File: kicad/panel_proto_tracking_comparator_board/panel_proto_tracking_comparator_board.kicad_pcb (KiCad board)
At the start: 2 copper layers, 102 x 67.5 mm, 570 parts, among them U1 TLV3542, U2 MCP6566

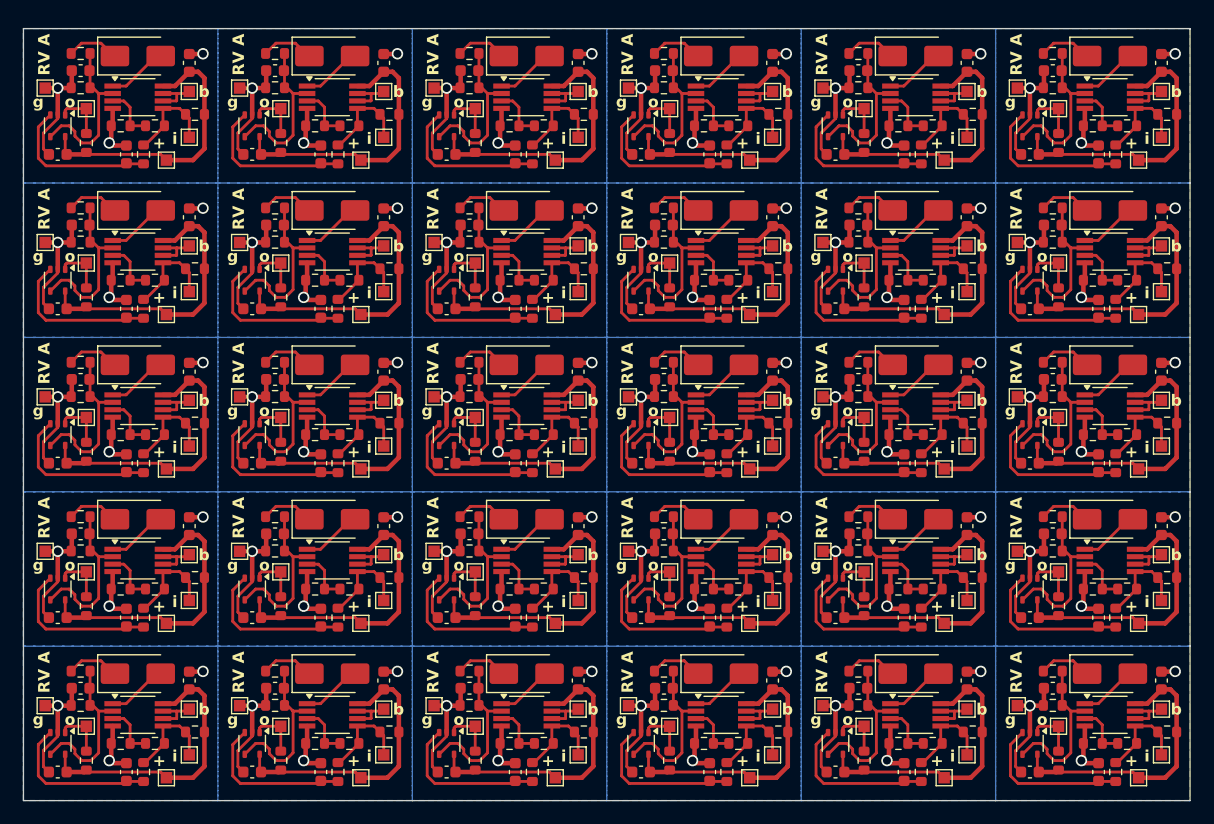
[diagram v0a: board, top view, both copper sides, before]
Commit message: Save bodge board rev B and additional sims
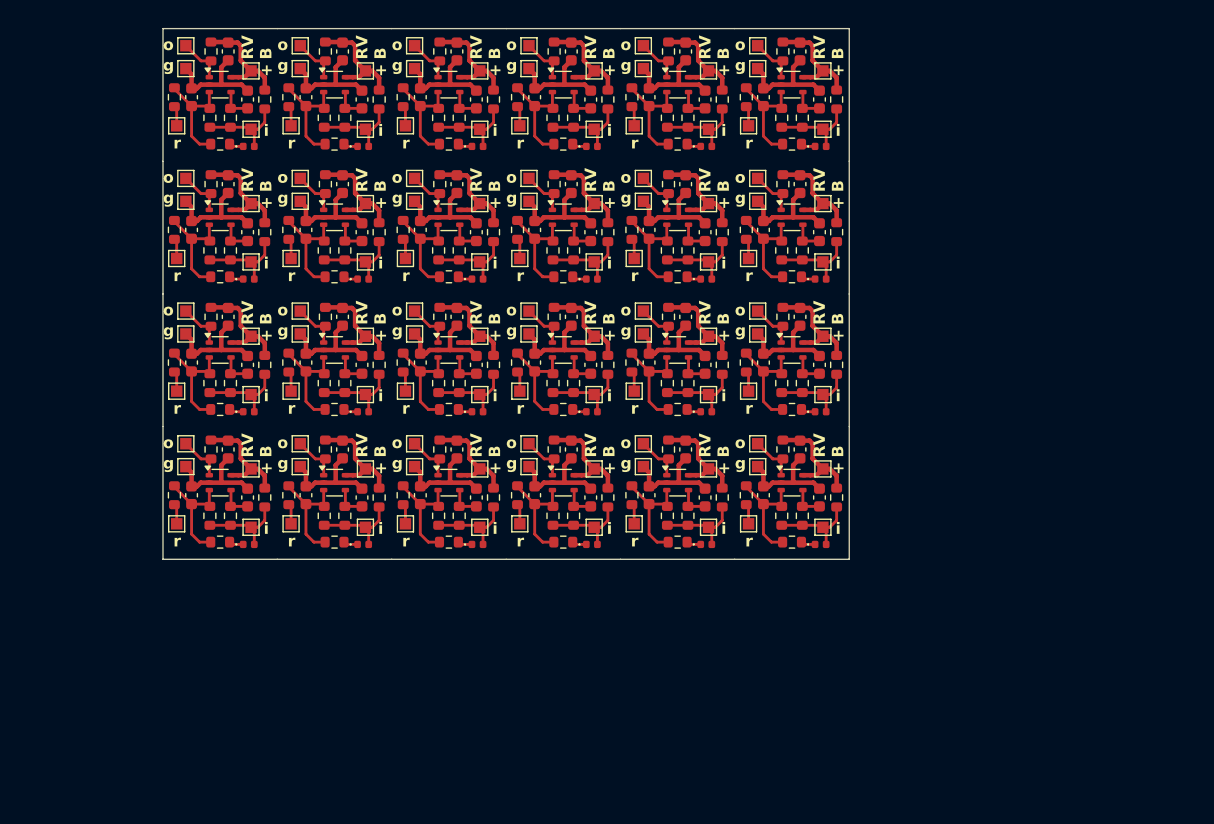
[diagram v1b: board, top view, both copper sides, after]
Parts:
- removed the C1 at (146.0, 23.0)
- removed the C1 at (197.0, 50.0)
- removed the C1 at (163.0, 36.5)
- removed the C1 at (112.0, 77.0)
- removed the C1 at (163.0, 50.0)
- removed the C1 at (163.0, 63.5)
- removed the C1 at (146.0, 63.5)
- removed the C1 at (180.0, 77.0)
- removed the C1 at (146.0, 77.0)
- removed the C1 at (163.0, 77.0)
- removed the C1 at (146.0, 36.5)
- removed the C1 at (197.0, 36.5)
- removed the C1 at (146.0, 50.0)
- removed the C1 at (129.0, 77.0)
- removed the C1 at (129.0, 36.5)
- removed the C1 at (197.0, 63.5)
- removed the C1 at (163.0, 23.0)
- removed the C1 at (112.0, 63.5)
- removed the C1 at (112.0, 23.0)
- removed the C1 at (180.0, 23.0)
- removed the C1 at (197.0, 23.0)
- removed the C1 at (129.0, 50.0)
- removed the C1 at (112.0, 50.0)
- removed the C1 at (180.0, 63.5)
- removed the C1 at (180.0, 50.0)
- removed the C1 at (129.0, 23.0)
- removed the C1 at (129.0, 63.5)
- removed the C1 at (197.0, 77.0)
- removed the C1 at (112.0, 36.5)
- removed the C1 at (180.0, 36.5)
- removed the C2 at (153.5, 77.7)
- removed the C2 at (136.5, 23.7)
- removed the C2 at (170.5, 50.7)
- removed the C2 at (102.5, 64.2)
- removed the C2 at (119.5, 50.7)
- removed the C2 at (102.5, 50.7)
- removed the C2 at (170.5, 77.7)
- removed the C2 at (102.5, 37.2)
- removed the C2 at (187.5, 77.7)
- removed the C2 at (153.5, 23.7)
- removed the C2 at (170.5, 23.7)
- removed the C2 at (187.5, 50.7)
- removed the C2 at (119.5, 64.2)
- removed the C2 at (170.5, 64.2)
- removed the C2 at (153.5, 37.2)
- removed the C2 at (119.5, 23.7)
- removed the C2 at (187.5, 23.7)
- removed the C2 at (136.5, 64.2)
- removed the C2 at (187.5, 37.2)
- removed the C2 at (102.5, 23.7)
- removed the C2 at (136.5, 50.7)
- removed the C2 at (153.5, 64.2)
- removed the C2 at (136.5, 37.2)
- removed the C2 at (102.5, 77.7)
- removed the C2 at (153.5, 50.7)
- removed the C2 at (119.5, 77.7)
- removed the C2 at (187.5, 64.2)
- removed the C2 at (170.5, 37.2)
- removed the C2 at (119.5, 37.2)
- removed the C2 at (136.5, 77.7)
- removed the C3 at (191.5, 71.5)
- removed the C3 at (157.5, 71.5)
- removed the C3 at (174.5, 44.5)
- removed the C3 at (174.5, 85.0)
- removed the C3 at (123.5, 31.0)
- removed the C3 at (106.5, 31.0)
- removed the C3 at (157.5, 44.5)
- removed the C3 at (191.5, 31.0)
- removed the C3 at (123.5, 71.5)
- removed the C3 at (140.5, 85.0)
- removed the C3 at (174.5, 31.0)
- removed the C3 at (174.5, 58.0)
- removed the C3 at (174.5, 71.5)
- removed the C3 at (140.5, 31.0)
- removed the C3 at (191.5, 85.0)
- removed the C3 at (106.5, 71.5)
- removed the C3 at (191.5, 44.5)
- removed the C3 at (123.5, 58.0)
- removed the C3 at (157.5, 31.0)
- removed the C3 at (123.5, 85.0)
- removed the C3 at (106.5, 58.0)
- removed the C3 at (106.5, 85.0)
- removed the C3 at (140.5, 44.5)
- removed the C3 at (157.5, 58.0)
- removed the C3 at (157.5, 85.0)
- removed the C3 at (140.5, 58.0)
- removed the C3 at (123.5, 44.5)
- removed the C3 at (191.5, 58.0)
- removed the C3 at (106.5, 44.5)
- removed the C3 at (140.5, 71.5)
- removed C4 (x30): 0.1uF, Capacitor_SMD:C_0603_1608Metric
- removed the D1 at (158.5, 62.9)
- removed the D1 at (175.5, 76.4)
- removed the D1 at (175.5, 49.4)
- removed the D1 at (192.5, 22.4)
- removed the D1 at (141.5, 62.9)
- removed the D1 at (158.5, 35.9)
- removed the D1 at (124.5, 76.4)
- removed the D1 at (124.5, 22.4)
- removed the D1 at (107.5, 49.4)
- removed the D1 at (192.5, 76.4)
- removed the D1 at (158.5, 22.4)
- removed the D1 at (192.5, 62.9)
- removed the D1 at (124.5, 49.4)
- removed the D1 at (192.5, 35.9)
- removed the D1 at (141.5, 22.4)
- removed the D1 at (124.5, 35.9)
- removed the D1 at (175.5, 22.4)
- removed the D1 at (175.5, 62.9)
- removed the D1 at (192.5, 49.4)
- removed the D1 at (141.5, 76.4)
- removed the D1 at (141.5, 35.9)
- removed the D1 at (141.5, 49.4)
- removed the D1 at (107.5, 62.9)
- removed the D1 at (107.5, 35.9)
- removed the D1 at (107.5, 22.4)
- removed the D1 at (158.5, 49.4)
- removed the D1 at (175.5, 35.9)
- removed the D1 at (158.5, 76.4)
- removed the D1 at (124.5, 62.9)
- removed the D1 at (107.5, 76.4)
- removed the R1 at (129.5, 27.5)
- removed the R1 at (180.5, 41.0)
- removed the R1 at (163.5, 27.5)
- removed the R1 at (197.5, 41.0)
- removed the R1 at (112.5, 41.0)
- removed the R1 at (163.5, 68.0)
- removed the R1 at (197.5, 68.0)
- removed the R1 at (129.5, 41.0)
- removed the R1 at (112.5, 68.0)
- removed the R1 at (146.5, 81.5)
- removed the R1 at (197.5, 54.5)
- removed the R1 at (197.5, 81.5)
- removed the R1 at (129.5, 81.5)
- removed the R1 at (146.5, 41.0)
- removed the R1 at (180.5, 68.0)
- removed the R1 at (146.5, 27.5)
- removed the R1 at (112.5, 27.5)
- removed the R1 at (180.5, 81.5)
- removed the R1 at (163.5, 54.5)
- removed the R1 at (163.5, 81.5)
- removed the R1 at (112.5, 81.5)
- removed the R1 at (163.5, 41.0)
- removed the R1 at (146.5, 54.5)
- removed the R1 at (180.5, 54.5)
- removed the R1 at (129.5, 54.5)
- removed the R1 at (197.5, 27.5)
- removed the R1 at (180.5, 27.5)
- removed the R1 at (129.5, 68.0)
- removed the R1 at (146.5, 68.0)
- removed the R1 at (112.5, 54.5)
- removed the R2 at (126.0, 82.5)
- removed the R2 at (126.0, 42.0)
- removed the R2 at (194.0, 42.0)
- removed the R2 at (109.0, 28.5)
- removed the R2 at (177.0, 42.0)
- removed the R2 at (126.0, 69.0)
- removed the R2 at (160.0, 28.5)
- removed the R2 at (143.0, 55.5)
- removed the R2 at (109.0, 69.0)
- removed the R2 at (143.0, 69.0)
- removed the R2 at (126.0, 55.5)
- removed the R2 at (160.0, 42.0)
- removed the R2 at (126.0, 28.5)
- removed the R2 at (143.0, 42.0)
- removed the R2 at (109.0, 42.0)
- removed the R2 at (177.0, 82.5)
- removed the R2 at (109.0, 55.5)
- removed the R2 at (160.0, 82.5)
- removed the R2 at (194.0, 28.5)
- removed the R2 at (143.0, 28.5)
- removed the R2 at (194.0, 69.0)
- removed the R2 at (177.0, 69.0)
- removed the R2 at (177.0, 28.5)
- removed the R2 at (109.0, 82.5)
- removed the R2 at (160.0, 69.0)
- removed the R2 at (160.0, 55.5)
- removed the R2 at (194.0, 82.5)
- removed the R2 at (143.0, 82.5)
- removed the R2 at (177.0, 55.5)
- removed the R2 at (194.0, 55.5)
- removed the R3 at (157.0, 28.5)
- removed the R3 at (106.0, 42.0)
- removed the R3 at (123.0, 28.5)
- removed the R3 at (191.0, 28.5)
- removed the R3 at (140.0, 42.0)
- removed the R3 at (157.0, 42.0)
- removed the R3 at (157.0, 69.0)
- removed the R3 at (174.0, 69.0)
- removed the R3 at (140.0, 55.5)
- removed the R3 at (191.0, 55.5)
- removed the R3 at (157.0, 82.5)
- removed the R3 at (106.0, 69.0)
- removed the R3 at (157.0, 55.5)
- removed the R3 at (106.0, 55.5)
- removed the R3 at (191.0, 42.0)
- removed the R3 at (140.0, 28.5)
- removed the R3 at (123.0, 69.0)
- removed the R3 at (191.0, 69.0)
- removed the R3 at (123.0, 42.0)
- removed the R3 at (140.0, 82.5)
- removed the R3 at (191.0, 82.5)
- removed the R3 at (174.0, 55.5)
- removed the R3 at (106.0, 82.5)
- removed the R3 at (123.0, 55.5)
- removed the R3 at (174.0, 82.5)
- removed the R3 at (106.0, 28.5)
- removed the R3 at (123.0, 82.5)
- removed the R3 at (174.0, 28.5)
- removed the R3 at (140.0, 69.0)
- removed the R3 at (174.0, 42.0)
- removed the R4 at (119.5, 35.7)
- removed the R4 at (102.5, 49.2)
- removed the R4 at (170.5, 35.7)
- removed the R4 at (136.5, 35.7)
- removed the R4 at (170.5, 62.7)
- removed the R4 at (136.5, 62.7)
- removed the R4 at (136.5, 49.2)
- removed the R4 at (119.5, 62.7)
- removed the R4 at (187.5, 62.7)
- removed the R4 at (119.5, 22.2)
- removed the R4 at (153.5, 62.7)
- removed the R4 at (102.5, 76.2)
- removed the R4 at (170.5, 22.2)
- removed the R4 at (119.5, 49.2)
- removed the R4 at (136.5, 22.2)
- removed the R4 at (153.5, 49.2)
- removed the R4 at (153.5, 35.7)
- removed the R4 at (187.5, 22.2)
- removed the R4 at (136.5, 76.2)
- removed the R4 at (170.5, 76.2)
- removed the R4 at (153.5, 22.2)
- removed the R4 at (102.5, 62.7)
- removed the R4 at (187.5, 35.7)
- removed the R4 at (187.5, 49.2)
- removed the R4 at (102.5, 35.7)
- removed the R4 at (187.5, 76.2)
- removed the R4 at (102.5, 22.2)
- removed the R4 at (153.5, 76.2)
- removed the R4 at (170.5, 49.2)
- removed the R4 at (119.5, 76.2)
- removed the R5 at (170.5, 25.2)
- removed the R5 at (187.5, 25.2)
- removed the R5 at (102.5, 25.2)
- removed the R5 at (153.5, 38.7)
- removed the R5 at (170.5, 52.2)
- removed the R5 at (102.5, 52.2)
- removed the R5 at (153.5, 52.2)
- removed the R5 at (153.5, 65.7)
- removed the R5 at (187.5, 65.7)
- removed the R5 at (119.5, 38.7)
- removed the R5 at (102.5, 79.2)
- removed the R5 at (187.5, 38.7)
- removed the R5 at (119.5, 25.2)
- removed the R5 at (170.5, 65.7)
- removed the R5 at (102.5, 38.7)
- removed the R5 at (187.5, 52.2)
- removed the R5 at (119.5, 79.2)
- removed the R5 at (187.5, 79.2)
- removed the R5 at (136.5, 65.7)
- removed the R5 at (119.5, 52.2)
- removed the R5 at (136.5, 38.7)
- removed the R5 at (170.5, 38.7)
- removed the R5 at (136.5, 79.2)
- removed the R5 at (102.5, 65.7)
- removed the R5 at (153.5, 25.2)
- removed the R5 at (136.5, 52.2)
- removed the R5 at (119.5, 65.7)
- removed the R5 at (153.5, 79.2)
- removed the R5 at (170.5, 79.2)
- removed the R5 at (136.5, 25.2)
- removed the R6 at (108.0, 44.5)
- removed the R6 at (159.0, 44.5)
- removed the R6 at (159.0, 85.0)
- removed the R6 at (108.0, 85.0)
- removed the R6 at (142.0, 85.0)
- removed the R6 at (176.0, 31.0)
- removed the R6 at (193.0, 58.0)
- removed the R6 at (108.0, 58.0)
- removed the R6 at (125.0, 44.5)
- removed the R6 at (159.0, 71.5)
- removed the R6 at (193.0, 71.5)
- removed the R6 at (125.0, 58.0)
- removed the R6 at (142.0, 44.5)
- removed the R6 at (108.0, 31.0)
- removed the R6 at (193.0, 44.5)
- removed the R6 at (159.0, 58.0)
- removed the R6 at (125.0, 31.0)
- removed the R6 at (159.0, 31.0)
- removed the R6 at (176.0, 58.0)
- removed the R6 at (142.0, 31.0)
- removed the R6 at (125.0, 85.0)
- removed the R6 at (176.0, 85.0)
- removed the R6 at (176.0, 44.5)
- removed the R6 at (193.0, 85.0)
- removed the R6 at (125.0, 71.5)
- removed the R6 at (176.0, 71.5)
- removed the R6 at (108.0, 71.5)
- removed the R6 at (142.0, 71.5)
- removed the R6 at (193.0, 31.0)
- removed the R6 at (142.0, 58.0)
- removed R7 (x30): 1k, Resistor_SMD:R_0603_1608Metric
- removed the TP1 at (180.0, 56.5)
- removed the TP1 at (197.0, 70.0)
- removed the TP1 at (129.0, 83.5)
- removed the TP1 at (163.0, 56.5)
- removed the TP1 at (197.0, 56.5)
- removed the TP1 at (112.0, 56.5)
- removed the TP1 at (112.0, 83.5)
- removed the TP1 at (163.0, 83.5)
- removed the TP1 at (197.0, 43.0)
- removed the TP1 at (129.0, 43.0)
- removed the TP1 at (146.0, 29.5)
- removed the TP1 at (163.0, 29.5)
- removed the TP1 at (112.0, 29.5)
- removed the TP1 at (180.0, 29.5)
- removed the TP1 at (129.0, 56.5)
- removed the TP1 at (180.0, 43.0)
- removed the TP1 at (163.0, 70.0)
- removed the TP1 at (197.0, 29.5)
- removed the TP1 at (146.0, 83.5)
- removed the TP1 at (163.0, 43.0)
- removed the TP1 at (112.0, 43.0)
- removed the TP1 at (146.0, 70.0)
- removed the TP1 at (180.0, 70.0)
- removed the TP1 at (197.0, 83.5)
- removed the TP1 at (146.0, 56.5)
- removed the TP1 at (180.0, 83.5)
- removed the TP1 at (112.0, 70.0)
- removed the TP1 at (146.0, 43.0)
- removed the TP1 at (129.0, 70.0)
- removed the TP1 at (129.0, 29.5)
- removed the TP2 at (154.0, 40.5)
- removed the TP2 at (188.0, 54.0)
- removed the TP2 at (120.0, 67.5)
- removed the TP2 at (171.0, 54.0)
- removed the TP2 at (137.0, 54.0)
- removed the TP2 at (188.0, 81.0)
- removed the TP2 at (171.0, 67.5)
- removed the TP2 at (137.0, 81.0)
- removed the TP2 at (154.0, 27.0)
- removed the TP2 at (120.0, 81.0)
- removed the TP2 at (171.0, 40.5)
- removed the TP2 at (154.0, 67.5)
- removed the TP2 at (103.0, 40.5)
- removed the TP2 at (188.0, 27.0)
- removed the TP2 at (103.0, 27.0)
- removed the TP2 at (188.0, 40.5)
- removed the TP2 at (103.0, 81.0)
- removed the TP2 at (137.0, 27.0)
- removed the TP2 at (120.0, 54.0)
- removed the TP2 at (188.0, 67.5)
- removed the TP2 at (120.0, 27.0)
- removed the TP2 at (120.0, 40.5)
- removed the TP2 at (154.0, 54.0)
- removed the TP2 at (103.0, 67.5)
- removed the TP2 at (171.0, 27.0)
- removed the TP2 at (171.0, 81.0)
- removed the TP2 at (154.0, 81.0)
- removed the TP2 at (137.0, 40.5)
- removed the TP2 at (103.0, 54.0)
- removed the TP2 at (137.0, 67.5)
- removed the TP3 at (161.0, 31.5)
- removed the TP3 at (178.0, 45.0)
- removed the TP3 at (195.0, 85.5)
- removed the TP3 at (110.0, 45.0)
- removed the TP3 at (144.0, 72.0)
- removed the TP3 at (110.0, 85.5)
- removed the TP3 at (144.0, 85.5)
- removed the TP3 at (127.0, 31.5)
- removed the TP3 at (161.0, 45.0)
- removed the TP3 at (144.0, 45.0)
- removed the TP3 at (161.0, 85.5)
- removed the TP3 at (178.0, 85.5)
- removed the TP3 at (144.0, 58.5)
- removed the TP3 at (110.0, 58.5)
- removed the TP3 at (195.0, 72.0)
- removed the TP3 at (144.0, 31.5)
- removed the TP3 at (127.0, 72.0)
- removed the TP3 at (195.0, 58.5)
- removed the TP3 at (127.0, 85.5)
- removed the TP3 at (178.0, 72.0)
- removed the TP3 at (178.0, 58.5)
- removed the TP3 at (178.0, 31.5)
- removed the TP3 at (195.0, 45.0)
- removed the TP3 at (161.0, 58.5)
- removed the TP3 at (161.0, 72.0)
- removed the TP3 at (110.0, 72.0)
- removed the TP3 at (127.0, 58.5)
- removed the TP3 at (110.0, 31.5)
- removed the TP3 at (195.0, 31.5)
- removed the TP3 at (127.0, 45.0)
- removed the TP4 at (116.4, 38.7)
- removed the TP4 at (150.4, 79.2)
- removed the TP4 at (116.4, 65.7)
- removed the TP4 at (116.4, 52.2)
- removed the TP4 at (150.4, 65.7)
- removed the TP4 at (99.4, 25.2)
- removed the TP4 at (133.4, 52.2)
- removed the TP4 at (167.4, 79.2)
- removed the TP4 at (99.4, 38.7)
- removed the TP4 at (116.4, 79.2)
- removed the TP4 at (184.4, 79.2)
- removed the TP4 at (150.4, 52.2)
- removed the TP4 at (99.4, 52.2)
- removed the TP4 at (184.4, 38.7)
- removed the TP4 at (167.4, 38.7)
- removed the TP4 at (99.4, 65.7)
- removed the TP4 at (133.4, 25.2)
- removed the TP4 at (167.4, 52.2)
- removed the TP4 at (99.4, 79.2)
- removed the TP4 at (133.4, 38.7)
- removed the TP4 at (150.4, 25.2)
- removed the TP4 at (184.4, 52.2)
- removed the TP4 at (167.4, 25.2)
- removed the TP4 at (133.4, 79.2)
- removed the TP4 at (116.4, 25.2)
- removed the TP4 at (167.4, 65.7)
- removed the TP4 at (133.4, 65.7)
- removed the TP4 at (150.4, 38.7)
- removed the TP4 at (184.4, 25.2)
- removed the TP4 at (184.4, 65.7)
- removed the TP5 at (163.0, 25.5)
- removed the TP5 at (146.0, 52.5)
- removed the TP5 at (163.0, 52.5)
- removed the TP5 at (197.0, 52.5)
- removed the TP5 at (129.0, 39.0)
- removed the TP5 at (180.0, 39.0)
- removed the TP5 at (129.0, 79.5)
- removed the TP5 at (129.0, 25.5)
- removed the TP5 at (197.0, 25.5)
- removed the TP5 at (129.0, 52.5)
- removed the TP5 at (180.0, 79.5)
- removed the TP5 at (112.0, 25.5)
- removed the TP5 at (180.0, 25.5)
- removed the TP5 at (146.0, 66.0)
- removed the TP5 at (197.0, 39.0)
- removed the TP5 at (112.0, 66.0)
- removed the TP5 at (197.0, 79.5)
- removed the TP5 at (129.0, 66.0)
- removed the TP5 at (180.0, 52.5)
- removed the TP5 at (112.0, 79.5)
- removed the TP5 at (146.0, 79.5)
- removed the TP5 at (146.0, 25.5)
- removed the TP5 at (146.0, 39.0)
- removed the TP5 at (163.0, 79.5)
- removed the TP5 at (163.0, 39.0)
- removed the TP5 at (163.0, 66.0)
- removed the TP5 at (197.0, 66.0)
- removed the TP5 at (180.0, 66.0)
- removed the TP5 at (112.0, 52.5)
- removed the TP5 at (112.0, 39.0)
- removed the U1 at (141.5, 80.0)
- removed the U1 at (124.5, 39.5)
- removed the U1 at (192.5, 66.5)
- removed the U1 at (158.5, 66.5)
- removed the U1 at (192.5, 26.0)
- removed the U1 at (158.5, 39.5)
- removed the U1 at (175.5, 80.0)
- removed the U1 at (107.5, 39.5)
- removed the U1 at (124.5, 66.5)
- removed the U1 at (107.5, 66.5)
- removed the U1 at (141.5, 53.0)
- removed the U1 at (158.5, 80.0)
- removed the U1 at (175.5, 53.0)
- removed the U1 at (175.5, 66.5)
- removed the U1 at (107.5, 53.0)
- removed the U1 at (124.5, 80.0)
- removed the U1 at (158.5, 53.0)
- removed the U1 at (192.5, 39.5)
- removed the U1 at (192.5, 80.0)
- removed the U1 at (124.5, 26.0)
- removed the U1 at (124.5, 53.0)
- removed the U1 at (175.5, 26.0)
- removed the U1 at (107.5, 26.0)
- removed the U1 at (192.5, 53.0)
- removed the U1 at (175.5, 39.5)
- removed the U1 at (141.5, 26.0)
- removed the U1 at (158.5, 26.0)
- removed the U1 at (107.5, 80.0)
- removed the U1 at (141.5, 39.5)
- removed the U1 at (141.5, 66.5)
- removed U2 (x30): MCP6566, Package_TO_SOT_SMD:SOT-353_SC-70-5
- added C1: 0.1uF, Capacitor_SMD:C_0603_1608Metric, F.Cu at (145.4, 33.6)
- added C1: 0.1uF, Capacitor_SMD:C_0603_1608Metric, F.Cu at (125.4, 22.0)
- added C1: 0.1uF, Capacitor_SMD:C_0603_1608Metric, F.Cu at (135.4, 33.6)
- added C1: 0.1uF, Capacitor_SMD:C_0603_1608Metric, F.Cu at (135.4, 56.8)
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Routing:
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- removed copper zone on B.Cu, net Board_0-GND
- removed copper zone on B.Cu, net Board_1-GND
- removed copper zone on B.Cu, net Board_10-GND
- removed copper zone on B.Cu, net Board_11-GND
- removed copper zone on B.Cu, net Board_12-GND
- removed copper zone on B.Cu, net Board_13-GND
- removed copper zone on B.Cu, net Board_14-GND
- removed copper zone on B.Cu, net Board_15-GND
- removed copper zone on B.Cu, net Board_16-GND
- removed copper zone on B.Cu, net Board_17-GND
- removed copper zone on B.Cu, net Board_18-GND
- removed copper zone on B.Cu, net Board_19-GND
- removed copper zone on B.Cu, net Board_2-GND
- removed copper zone on B.Cu, net Board_20-GND
- removed copper zone on B.Cu, net Board_21-GND
- removed copper zone on B.Cu, net Board_22-GND
- removed copper zone on B.Cu, net Board_23-GND
- removed copper zone on B.Cu, net Board_24-GND
- removed copper zone on B.Cu, net Board_25-GND
- removed copper zone on B.Cu, net Board_26-GND
- removed copper zone on B.Cu, net Board_27-GND
- removed copper zone on B.Cu, net Board_28-GND
- removed copper zone on B.Cu, net Board_29-GND
- removed copper zone on B.Cu, net Board_3-GND
- removed copper zone on B.Cu, net Board_4-GND
- removed copper zone on B.Cu, net Board_5-GND
- removed copper zone on B.Cu, net Board_6-GND
- removed copper zone on B.Cu, net Board_7-GND
- removed copper zone on B.Cu, net Board_8-GND
- removed copper zone on B.Cu, net Board_9-GND
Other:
- board size 102 x 67.5 mm -> 60 x 46.4 mm
- board text added: "RV B"
- board text added: "r"
- board text removed: "RV A"
- board text removed: "b"

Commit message: Data slicer rev A
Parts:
- removed the C1 at (145.4, 33.6)
- removed the C1 at (125.4, 22.0)
- removed the C1 at (135.4, 33.6)
- removed the C1 at (135.4, 56.8)
- removed the C1 at (135.4, 22.0)
- removed the C1 at (135.4, 45.2)
- removed the C1 at (155.4, 33.6)
- removed the C1 at (165.4, 56.8)
- removed the C1 at (115.4, 56.8)
- removed the C1 at (115.4, 45.2)
- removed the C1 at (125.4, 56.8)
- removed the C1 at (155.4, 22.0)
- removed the C1 at (145.4, 22.0)
- removed the C1 at (145.4, 45.2)
- removed the C1 at (155.4, 45.2)
- removed the C1 at (125.4, 33.6)
- removed the C1 at (125.4, 45.2)
- removed the C1 at (165.4, 22.0)
- removed the C1 at (165.4, 33.6)
- removed the C1 at (145.4, 56.8)
- removed the C1 at (155.4, 56.8)
- removed the C1 at (115.4, 22.0)
- removed the C1 at (165.4, 45.2)
- removed the C1 at (115.4, 33.6)
- removed C2 (x24): 100pF, Capacitor_SMD:C_0603_1608Metric
- removed the C3 at (147.1, 49.4)
- removed the C3 at (127.1, 49.4)
- removed the C3 at (157.1, 61.0)
- removed the C3 at (137.1, 26.2)
- removed the C3 at (167.1, 26.2)
- removed the C3 at (157.1, 37.8)
- removed the C3 at (147.1, 61.0)
- removed the C3 at (167.1, 49.4)
- removed the C3 at (127.1, 26.2)
- removed the C3 at (167.1, 37.8)
- removed the C3 at (127.1, 61.0)
- removed the C3 at (137.1, 49.4)
- removed the C3 at (137.1, 61.0)
- removed the C3 at (147.1, 37.8)
- removed the C3 at (117.1, 61.0)
- removed the C3 at (167.1, 61.0)
- removed the C3 at (117.1, 26.2)
- removed the C3 at (127.1, 37.8)
- removed the C3 at (137.1, 37.8)
- removed the C3 at (117.1, 37.8)
- removed the C3 at (157.1, 49.4)
- removed the C3 at (157.1, 26.2)
- removed the C3 at (117.1, 49.4)
- removed the C3 at (147.1, 26.2)
- removed the D1 at (157.2, 30.3)
- removed the D1 at (137.2, 30.3)
- removed the D1 at (137.2, 53.5)
- removed the D1 at (167.2, 30.3)
- removed the D1 at (127.2, 41.9)
- removed the D1 at (127.2, 30.3)
- removed the D1 at (117.2, 41.9)
- removed the D1 at (167.2, 65.1)
- removed the D1 at (117.2, 65.1)
- removed the D1 at (167.2, 41.9)
- removed the D1 at (117.2, 30.3)
- removed the D1 at (117.2, 53.5)
- removed the D1 at (127.2, 65.1)
- removed the D1 at (157.2, 41.9)
- removed the D1 at (147.2, 65.1)
- removed the D1 at (157.2, 53.5)
- removed the D1 at (127.2, 53.5)
- removed the D1 at (157.2, 65.1)
- removed the D1 at (137.2, 65.1)
- removed the D1 at (137.2, 41.9)
- removed the D1 at (147.2, 41.9)
- removed the D1 at (147.2, 53.5)
- removed the D1 at (167.2, 53.5)
- removed the D1 at (147.2, 30.3)
- removed the R1 at (163.8, 51.0)
- removed the R1 at (143.8, 62.6)
- removed the R1 at (143.8, 51.0)
- removed the R1 at (133.8, 39.4)
- removed the R1 at (113.8, 51.0)
- removed the R1 at (133.8, 51.0)
- removed the R1 at (123.8, 51.0)
- removed the R1 at (163.8, 62.6)
- removed the R1 at (153.8, 39.4)
- removed the R1 at (113.8, 39.4)
- removed the R1 at (133.8, 27.8)
- removed the R1 at (123.8, 62.6)
- removed the R1 at (153.8, 51.0)
- removed the R1 at (123.8, 27.8)
- removed the R1 at (153.8, 62.6)
- removed the R1 at (113.8, 27.8)
- removed the R1 at (123.8, 39.4)
- removed the R1 at (143.8, 27.8)
- removed the R1 at (163.8, 27.8)
- removed the R1 at (133.8, 62.6)
- removed the R1 at (163.8, 39.4)
- removed the R1 at (143.8, 39.4)
- removed the R1 at (153.8, 27.8)
- removed the R1 at (113.8, 62.6)
- removed the R2 at (128.6, 26.2)
- removed the R2 at (118.6, 49.4)
- removed the R2 at (158.6, 37.8)
- removed the R2 at (168.6, 49.4)
- removed the R2 at (118.6, 26.2)
- removed the R2 at (118.6, 37.8)
- removed the R2 at (138.6, 61.0)
- removed the R2 at (158.6, 26.2)
- removed the R2 at (168.6, 26.2)
- removed the R2 at (148.6, 49.4)
- removed the R2 at (128.6, 37.8)
- removed the R2 at (168.6, 37.8)
- removed the R2 at (158.6, 49.4)
- removed the R2 at (128.6, 49.4)
- removed the R2 at (148.6, 61.0)
- removed the R2 at (148.6, 37.8)
- removed the R2 at (138.6, 49.4)
- removed the R2 at (128.6, 61.0)
- removed the R2 at (158.6, 61.0)
- removed the R2 at (138.6, 26.2)
- removed the R2 at (148.6, 26.2)
- removed the R2 at (168.6, 61.0)
- removed the R2 at (118.6, 61.0)
- removed the R2 at (138.6, 37.8)
- removed R3 (x24): 1k, Resistor_SMD:R_0603_1608Metric
- removed R4 (x24): 10k, Resistor_SMD:R_0603_1608Metric
- removed the R5 at (135.6, 51.0)
- removed the R5 at (145.6, 62.6)
- removed the R5 at (165.6, 39.4)
- removed the R5 at (155.6, 51.0)
- removed the R5 at (135.6, 39.4)
- removed the R5 at (115.6, 27.8)
- removed the R5 at (155.6, 27.8)
- removed the R5 at (115.6, 51.0)
- removed the R5 at (115.6, 62.6)
- removed the R5 at (115.6, 39.4)
- removed the R5 at (165.6, 51.0)
- removed the R5 at (155.6, 62.6)
- removed the R5 at (145.6, 51.0)
- removed the R5 at (125.6, 51.0)
- removed the R5 at (125.6, 62.6)
- removed the R5 at (135.6, 27.8)
- removed the R5 at (135.6, 62.6)
- removed the R5 at (145.6, 39.4)
- removed the R5 at (125.6, 27.8)
- removed the R5 at (165.6, 62.6)
- removed the R5 at (145.6, 27.8)
- removed the R5 at (165.6, 27.8)
- removed the R5 at (155.6, 39.4)
- removed the R5 at (125.6, 39.4)
- removed R6 (x24): 1M, Resistor_SMD:R_0603_1608Metric
- removed the TP1 at (157.4, 40.4)
- removed the TP1 at (117.4, 63.6)
- removed the TP1 at (137.4, 40.4)
- removed the TP1 at (117.4, 52.0)
- removed the TP1 at (167.4, 52.0)
- removed the TP1 at (147.4, 40.4)
- removed the TP1 at (127.4, 52.0)
- removed the TP1 at (167.4, 40.4)
- removed the TP1 at (147.4, 28.8)
- removed the TP1 at (127.4, 28.8)
- removed the TP1 at (117.4, 40.4)
- removed the TP1 at (127.4, 40.4)
- removed the TP1 at (147.4, 52.0)
- removed the TP1 at (137.4, 28.8)
- removed the TP1 at (117.4, 28.8)
- removed the TP1 at (157.4, 52.0)
- removed the TP1 at (167.4, 63.6)
- removed the TP1 at (167.4, 28.8)
- removed the TP1 at (137.4, 52.0)
- removed the TP1 at (157.4, 63.6)
- removed the TP1 at (157.4, 28.8)
- removed the TP1 at (127.4, 63.6)
- removed the TP1 at (147.4, 63.6)
- removed the TP1 at (137.4, 63.6)
- removed the TP2 at (151.7, 56.3)
- removed the TP2 at (151.7, 33.1)
- removed the TP2 at (121.7, 21.5)
- removed the TP2 at (111.7, 33.1)
- removed the TP2 at (141.7, 44.7)
- removed the TP2 at (131.7, 33.1)
- removed the TP2 at (151.7, 21.5)
- removed the TP2 at (161.7, 33.1)
- removed the TP2 at (141.7, 21.5)
- removed the TP2 at (141.7, 56.3)
- removed the TP2 at (121.7, 44.7)
- removed the TP2 at (151.7, 44.7)
- removed the TP2 at (141.7, 33.1)
- removed the TP2 at (161.7, 44.7)
- removed the TP2 at (131.7, 21.5)
- removed the TP2 at (121.7, 56.3)
- removed the TP2 at (111.7, 44.7)
- removed the TP2 at (121.7, 33.1)
- removed the TP2 at (131.7, 56.3)
- removed the TP2 at (111.7, 21.5)
- removed the TP2 at (161.7, 21.5)
- removed the TP2 at (111.7, 56.3)
- removed the TP2 at (131.7, 44.7)
- removed the TP2 at (161.7, 56.3)
- removed TP3 (x24): TestPoint, TestPoint:TestPoint_Pad_1.0x1.0mm
- removed the TP4 at (161.7, 46.7)
- removed the TP4 at (131.7, 58.3)
- removed the TP4 at (131.7, 46.7)
- removed the TP4 at (161.7, 23.5)
- removed the TP4 at (151.7, 46.7)
- removed the TP4 at (161.7, 35.1)
- removed the TP4 at (131.7, 23.5)
- removed the TP4 at (131.7, 35.1)
- removed the TP4 at (111.7, 58.3)
- removed the TP4 at (141.7, 46.7)
- removed the TP4 at (141.7, 35.1)
- removed the TP4 at (151.7, 58.3)
- removed the TP4 at (111.7, 35.1)
- removed the TP4 at (121.7, 58.3)
- removed the TP4 at (141.7, 58.3)
- removed the TP4 at (121.7, 35.1)
- removed the TP4 at (151.7, 35.1)
- removed the TP4 at (141.7, 23.5)
- removed the TP4 at (161.7, 58.3)
- removed the TP4 at (111.7, 46.7)
- removed the TP4 at (121.7, 23.5)
- removed the TP4 at (151.7, 23.5)
- removed the TP4 at (111.7, 23.5)
- removed the TP4 at (121.7, 46.7)
- removed the TP5 at (140.9, 28.5)
- removed the TP5 at (150.9, 51.7)
- removed the TP5 at (160.9, 40.1)
- removed the TP5 at (120.9, 40.1)
- removed the TP5 at (120.9, 28.5)
- removed the TP5 at (130.9, 63.3)
- removed the TP5 at (140.9, 40.1)
- removed the TP5 at (110.9, 63.3)
- removed the TP5 at (130.9, 51.7)
- removed the TP5 at (110.9, 40.1)
- removed the TP5 at (130.9, 28.5)
- removed the TP5 at (110.9, 51.7)
- removed the TP5 at (140.9, 51.7)
- removed the TP5 at (160.9, 63.3)
- removed the TP5 at (120.9, 51.7)
- removed the TP5 at (160.9, 28.5)
- removed the TP5 at (150.9, 28.5)
- removed the TP5 at (140.9, 63.3)
- removed the TP5 at (120.9, 63.3)
- removed the TP5 at (130.9, 40.1)
- removed the TP5 at (150.9, 63.3)
- removed the TP5 at (160.9, 51.7)
- removed the TP5 at (110.9, 28.5)
- removed the TP5 at (150.9, 40.1)
- removed U1 (x24): MCP6566, Package_TO_SOT_SMD:SOT-353_SC-70-5
- added C1: 0.1uF, Capacitor_SMD:C_0603_1608Metric, F.Cu at (165.7, 41.0)
- added C1: 0.1uF, Capacitor_SMD:C_0603_1608Metric, F.Cu at (114.7, 33.5)
- added C1: 0.1uF, Capacitor_SMD:C_0603_1608Metric, F.Cu at (165.7, 56.0)
- added C1: 0.1uF, Capacitor_SMD:C_0603_1608Metric, F.Cu at (114.7, 41.0)
- added C1: 0.1uF, Capacitor_SMD:C_0603_1608Metric, F.Cu at (114.7, 63.5)
- added C1: 0.1uF, Capacitor_SMD:C_0603_1608Metric, F.Cu at (148.7, 33.5)
- added C1: 0.1uF, Capacitor_SMD:C_0603_1608Metric, F.Cu at (114.7, 56.0)
- added C1: 0.1uF, Capacitor_SMD:C_0603_1608Metric, F.Cu at (131.7, 41.0)
- added C1: 0.1uF, Capacitor_SMD:C_0603_1608Metric, F.Cu at (114.7, 48.5)
- added C1: 0.1uF, Capacitor_SMD:C_0603_1608Metric, F.Cu at (165.7, 26.0)
- added C1: 0.1uF, Capacitor_SMD:C_0603_1608Metric, F.Cu at (165.7, 48.5)
- added C1: 0.1uF, Capacitor_SMD:C_0603_1608Metric, F.Cu at (131.7, 48.5)
- added C1: 0.1uF, Capacitor_SMD:C_0603_1608Metric, F.Cu at (131.7, 33.5)
- added C1: 0.1uF, Capacitor_SMD:C_0603_1608Metric, F.Cu at (148.7, 63.5)
- added C1: 0.1uF, Capacitor_SMD:C_0603_1608Metric, F.Cu at (165.7, 33.5)
- added C1: 0.1uF, Capacitor_SMD:C_0603_1608Metric, F.Cu at (131.7, 63.5)
- added C1: 0.1uF, Capacitor_SMD:C_0603_1608Metric, F.Cu at (131.7, 56.0)
- added C1: 0.1uF, Capacitor_SMD:C_0603_1608Metric, F.Cu at (148.7, 48.5)
- added C1: 0.1uF, Capacitor_SMD:C_0603_1608Metric, F.Cu at (114.7, 26.0)
- added C1: 0.1uF, Capacitor_SMD:C_0603_1608Metric, F.Cu at (148.7, 26.0)
- added C1: 0.1uF, Capacitor_SMD:C_0603_1608Metric, F.Cu at (131.7, 26.0)
- added C1: 0.1uF, Capacitor_SMD:C_0603_1608Metric, F.Cu at (148.7, 56.0)
- added C1: 0.1uF, Capacitor_SMD:C_0603_1608Metric, F.Cu at (165.7, 63.5)
- added C1: 0.1uF, Capacitor_SMD:C_0603_1608Metric, F.Cu at (148.7, 41.0)
- added C3: 1nF, Capacitor_SMD:C_0603_1608Metric, F.Cu at (114.7, 32.0)
- added C3: 1nF, Capacitor_SMD:C_0603_1608Metric, F.Cu at (131.7, 47.0)
- added C3: 1nF, Capacitor_SMD:C_0603_1608Metric, F.Cu at (165.7, 32.0)
- added C3: 1nF, Capacitor_SMD:C_0603_1608Metric, F.Cu at (131.7, 32.0)
- added C3: 1nF, Capacitor_SMD:C_0603_1608Metric, F.Cu at (114.7, 47.0)
- added C3: 1nF, Capacitor_SMD:C_0603_1608Metric, F.Cu at (165.7, 62.0)
- added C3: 1nF, Capacitor_SMD:C_0603_1608Metric, F.Cu at (131.7, 24.5)
- added C3: 1nF, Capacitor_SMD:C_0603_1608Metric, F.Cu at (148.7, 47.0)
- added C3: 1nF, Capacitor_SMD:C_0603_1608Metric, F.Cu at (165.7, 39.5)
- added C3: 1nF, Capacitor_SMD:C_0603_1608Metric, F.Cu at (131.7, 62.0)
- added C3: 1nF, Capacitor_SMD:C_0603_1608Metric, F.Cu at (114.7, 54.5)
- added C3: 1nF, Capacitor_SMD:C_0603_1608Metric, F.Cu at (148.7, 54.5)
- added C3: 1nF, Capacitor_SMD:C_0603_1608Metric, F.Cu at (131.7, 54.5)
- added C3: 1nF, Capacitor_SMD:C_0603_1608Metric, F.Cu at (165.7, 24.5)
- added C3: 1nF, Capacitor_SMD:C_0603_1608Metric, F.Cu at (148.7, 62.0)
- added C3: 1nF, Capacitor_SMD:C_0603_1608Metric, F.Cu at (148.7, 39.5)
- added C3: 1nF, Capacitor_SMD:C_0603_1608Metric, F.Cu at (114.7, 62.0)
- added C3: 1nF, Capacitor_SMD:C_0603_1608Metric, F.Cu at (165.7, 47.0)
- added C3: 1nF, Capacitor_SMD:C_0603_1608Metric, F.Cu at (114.7, 39.5)
- added C3: 1nF, Capacitor_SMD:C_0603_1608Metric, F.Cu at (131.7, 39.5)
- added C3: 1nF, Capacitor_SMD:C_0603_1608Metric, F.Cu at (165.7, 54.5)
- added C3: 1nF, Capacitor_SMD:C_0603_1608Metric, F.Cu at (148.7, 24.5)
- added C3: 1nF, Capacitor_SMD:C_0603_1608Metric, F.Cu at (114.7, 24.5)
- added C3: 1nF, Capacitor_SMD:C_0603_1608Metric, F.Cu at (148.7, 32.0)
- added D1: D_Schottky, Custom_Diode:D_0402_1005Metric, F.Cu at (162.7, 53.0)
- added D1: D_Schottky, Custom_Diode:D_0402_1005Metric, F.Cu at (162.7, 60.5)
- added D1: D_Schottky, Custom_Diode:D_0402_1005Metric, F.Cu at (128.7, 30.5)
- added D1: D_Schottky, Custom_Diode:D_0402_1005Metric, F.Cu at (128.7, 23.0)
- added D1: D_Schottky, Custom_Diode:D_0402_1005Metric, F.Cu at (111.7, 60.5)
- added D1: D_Schottky, Custom_Diode:D_0402_1005Metric, F.Cu at (111.7, 30.5)
- added D1: D_Schottky, Custom_Diode:D_0402_1005Metric, F.Cu at (111.7, 38.0)
- added D1: D_Schottky, Custom_Diode:D_0402_1005Metric, F.Cu at (145.7, 23.0)
- added D1: D_Schottky, Custom_Diode:D_0402_1005Metric, F.Cu at (145.7, 30.5)
- added D1: D_Schottky, Custom_Diode:D_0402_1005Metric, F.Cu at (145.7, 38.0)
- added D1: D_Schottky, Custom_Diode:D_0402_1005Metric, F.Cu at (145.7, 45.5)
- added D1: D_Schottky, Custom_Diode:D_0402_1005Metric, F.Cu at (128.7, 38.0)
- added D1: D_Schottky, Custom_Diode:D_0402_1005Metric, F.Cu at (128.7, 60.5)
- added D1: D_Schottky, Custom_Diode:D_0402_1005Metric, F.Cu at (162.7, 30.5)
- added D1: D_Schottky, Custom_Diode:D_0402_1005Metric, F.Cu at (128.7, 53.0)
- added D1: D_Schottky, Custom_Diode:D_0402_1005Metric, F.Cu at (162.7, 45.5)
- added D1: D_Schottky, Custom_Diode:D_0402_1005Metric, F.Cu at (111.7, 23.0)
- added D1: D_Schottky, Custom_Diode:D_0402_1005Metric, F.Cu at (111.7, 45.5)
- added D1: D_Schottky, Custom_Diode:D_0402_1005Metric, F.Cu at (162.7, 38.0)
- added D1: D_Schottky, Custom_Diode:D_0402_1005Metric, F.Cu at (162.7, 23.0)
- added D1: D_Schottky, Custom_Diode:D_0402_1005Metric, F.Cu at (128.7, 45.5)
- added D1: D_Schottky, Custom_Diode:D_0402_1005Metric, F.Cu at (145.7, 60.5)
- added D1: D_Schottky, Custom_Diode:D_0402_1005Metric, F.Cu at (111.7, 53.0)
- added D1: D_Schottky, Custom_Diode:D_0402_1005Metric, F.Cu at (145.7, 53.0)
- added D2: D_Schottky, Custom_Diode:D_0402_1005Metric, F.Cu at (111.7, 54.5)
- added D2: D_Schottky, Custom_Diode:D_0402_1005Metric, F.Cu at (162.7, 54.5)
- added D2: D_Schottky, Custom_Diode:D_0402_1005Metric, F.Cu at (162.7, 24.5)
- added D2: D_Schottky, Custom_Diode:D_0402_1005Metric, F.Cu at (111.7, 24.5)
- added D2: D_Schottky, Custom_Diode:D_0402_1005Metric, F.Cu at (111.7, 47.0)
- added D2: D_Schottky, Custom_Diode:D_0402_1005Metric, F.Cu at (162.7, 62.0)
- added D2: D_Schottky, Custom_Diode:D_0402_1005Metric, F.Cu at (145.7, 39.5)
- added D2: D_Schottky, Custom_Diode:D_0402_1005Metric, F.Cu at (128.7, 24.5)
- added D2: D_Schottky, Custom_Diode:D_0402_1005Metric, F.Cu at (111.7, 62.0)
- added D2: D_Schottky, Custom_Diode:D_0402_1005Metric, F.Cu at (145.7, 24.5)
- added D2: D_Schottky, Custom_Diode:D_0402_1005Metric, F.Cu at (128.7, 54.5)
- added D2: D_Schottky, Custom_Diode:D_0402_1005Metric, F.Cu at (145.7, 32.0)
- added D2: D_Schottky, Custom_Diode:D_0402_1005Metric, F.Cu at (128.7, 62.0)
- added D2: D_Schottky, Custom_Diode:D_0402_1005Metric, F.Cu at (145.7, 54.5)
- added D2: D_Schottky, Custom_Diode:D_0402_1005Metric, F.Cu at (128.7, 39.5)
- added D2: D_Schottky, Custom_Diode:D_0402_1005Metric, F.Cu at (111.7, 32.0)
- added D2: D_Schottky, Custom_Diode:D_0402_1005Metric, F.Cu at (162.7, 39.5)
- added D2: D_Schottky, Custom_Diode:D_0402_1005Metric, F.Cu at (162.7, 47.0)
- added D2: D_Schottky, Custom_Diode:D_0402_1005Metric, F.Cu at (162.7, 32.0)
- added D2: D_Schottky, Custom_Diode:D_0402_1005Metric, F.Cu at (145.7, 62.0)
- added D2: D_Schottky, Custom_Diode:D_0402_1005Metric, F.Cu at (128.7, 32.0)
- added D2: D_Schottky, Custom_Diode:D_0402_1005Metric, F.Cu at (111.7, 39.5)
- added D2: D_Schottky, Custom_Diode:D_0402_1005Metric, F.Cu at (128.7, 47.0)
- added D2: D_Schottky, Custom_Diode:D_0402_1005Metric, F.Cu at (145.7, 47.0)
- added R1: 10k, Resistor_SMD:R_0603_1608Metric, F.Cu at (111.7, 48.5)
- added R1: 10k, Resistor_SMD:R_0603_1608Metric, F.Cu at (111.7, 56.0)
- added R1: 10k, Resistor_SMD:R_0603_1608Metric, F.Cu at (145.7, 26.0)
- added R1: 10k, Resistor_SMD:R_0603_1608Metric, F.Cu at (162.7, 48.5)
- added R1: 10k, Resistor_SMD:R_0603_1608Metric, F.Cu at (162.7, 56.0)
- added R1: 10k, Resistor_SMD:R_0603_1608Metric, F.Cu at (145.7, 33.5)
- added R1: 10k, Resistor_SMD:R_0603_1608Metric, F.Cu at (162.7, 63.5)
- added R1: 10k, Resistor_SMD:R_0603_1608Metric, F.Cu at (128.7, 26.0)
- added R1: 10k, Resistor_SMD:R_0603_1608Metric, F.Cu at (111.7, 63.5)
- added R1: 10k, Resistor_SMD:R_0603_1608Metric, F.Cu at (162.7, 26.0)
- added R1: 10k, Resistor_SMD:R_0603_1608Metric, F.Cu at (145.7, 63.5)
- added R1: 10k, Resistor_SMD:R_0603_1608Metric, F.Cu at (145.7, 56.0)
- added R1: 10k, Resistor_SMD:R_0603_1608Metric, F.Cu at (162.7, 33.5)
- added R1: 10k, Resistor_SMD:R_0603_1608Metric, F.Cu at (128.7, 33.5)
- added R1: 10k, Resistor_SMD:R_0603_1608Metric, F.Cu at (145.7, 48.5)
- added R1: 10k, Resistor_SMD:R_0603_1608Metric, F.Cu at (111.7, 33.5)
- added R1: 10k, Resistor_SMD:R_0603_1608Metric, F.Cu at (128.7, 41.0)
- added R1: 10k, Resistor_SMD:R_0603_1608Metric, F.Cu at (111.7, 26.0)
- added R1: 10k, Resistor_SMD:R_0603_1608Metric, F.Cu at (128.7, 48.5)
- added R1: 10k, Resistor_SMD:R_0603_1608Metric, F.Cu at (128.7, 56.0)
- added R1: 10k, Resistor_SMD:R_0603_1608Metric, F.Cu at (162.7, 41.0)
- added R1: 10k, Resistor_SMD:R_0603_1608Metric, F.Cu at (128.7, 63.5)
- added R1: 10k, Resistor_SMD:R_0603_1608Metric, F.Cu at (145.7, 41.0)
- added R1: 10k, Resistor_SMD:R_0603_1608Metric, F.Cu at (111.7, 41.0)
- added R2: 100k, Resistor_SMD:R_0603_1608Metric, F.Cu at (134.2, 29.5)
- added R2: 100k, Resistor_SMD:R_0603_1608Metric, F.Cu at (117.2, 29.5)
- added R2: 100k, Resistor_SMD:R_0603_1608Metric, F.Cu at (168.2, 52.0)
- added R2: 100k, Resistor_SMD:R_0603_1608Metric, F.Cu at (134.2, 37.0)
- added R2: 100k, Resistor_SMD:R_0603_1608Metric, F.Cu at (151.2, 59.5)
- added R2: 100k, Resistor_SMD:R_0603_1608Metric, F.Cu at (134.2, 59.5)
- added R2: 100k, Resistor_SMD:R_0603_1608Metric, F.Cu at (168.2, 37.0)
- added R2: 100k, Resistor_SMD:R_0603_1608Metric, F.Cu at (134.2, 44.5)
- added R2: 100k, Resistor_SMD:R_0603_1608Metric, F.Cu at (151.2, 29.5)
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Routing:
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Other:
- board size 60 x 46.4 mm -> 68 x 45 mm
- board text added: "RV C"
- board text added: "rl"
- board text added: "rs"
- board text added: "tf"
- board text added: "th"
- board text added: "tl"
- board text removed: "+"
- board text removed: "RV B"
- board text removed: "V-CUT"
- board text removed: "i"
- board text removed: "o"
- board text removed: "r"
